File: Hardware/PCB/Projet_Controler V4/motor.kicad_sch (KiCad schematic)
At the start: 5 parts, among them J601 Conn_01x02, Q601 SQ2310ES-T1

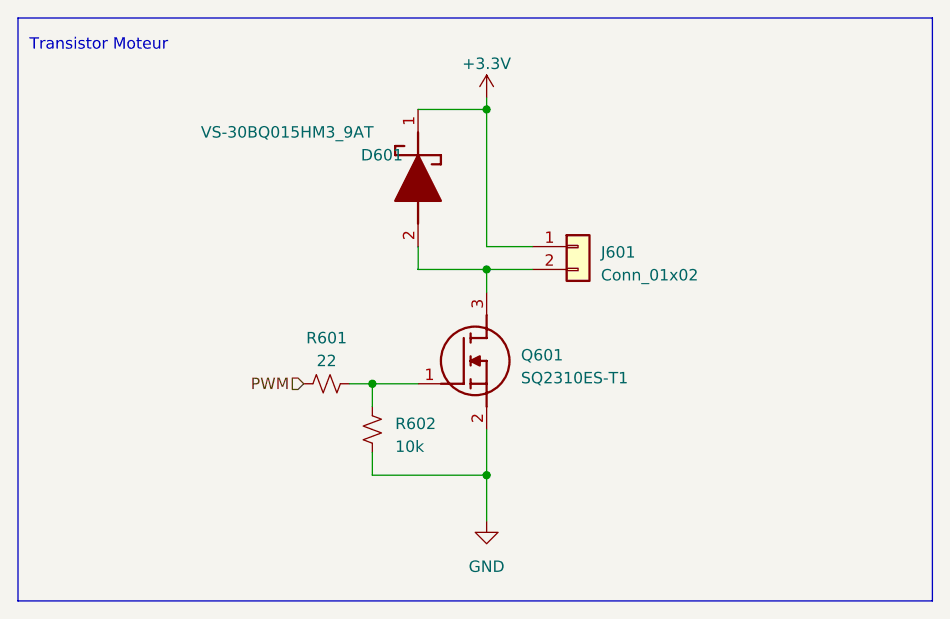
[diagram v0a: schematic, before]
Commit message: reroutage LF pas assumé à 100%
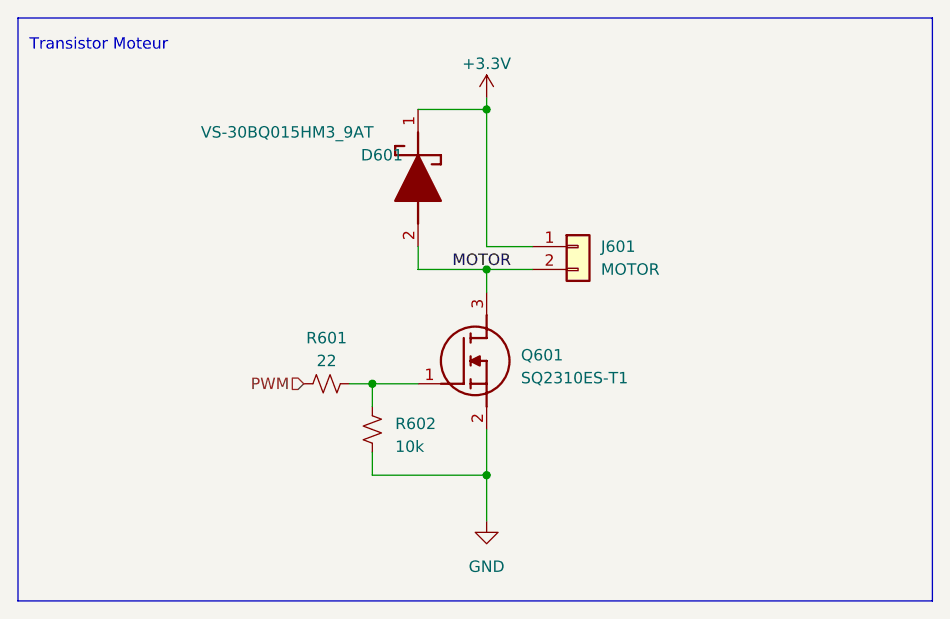
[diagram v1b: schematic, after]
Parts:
- J601: value Conn_01x02 -> MOTOR
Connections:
- net MOTOR: now reaches D601.2 (A), J601.2 (Pin_2), Q601.3 (D)
